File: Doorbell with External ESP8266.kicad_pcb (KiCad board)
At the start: 4 copper layers, 76.2 x 50.8 mm, 29 parts, among them J101 Rectifier, J105 Transformer, J106 Button, J107 Chime, K102 Relay, Q102 Q_NMOS_GSD, U101 WeMos_D1_mini, U102 EL817, U104 XC6220B331MR-G

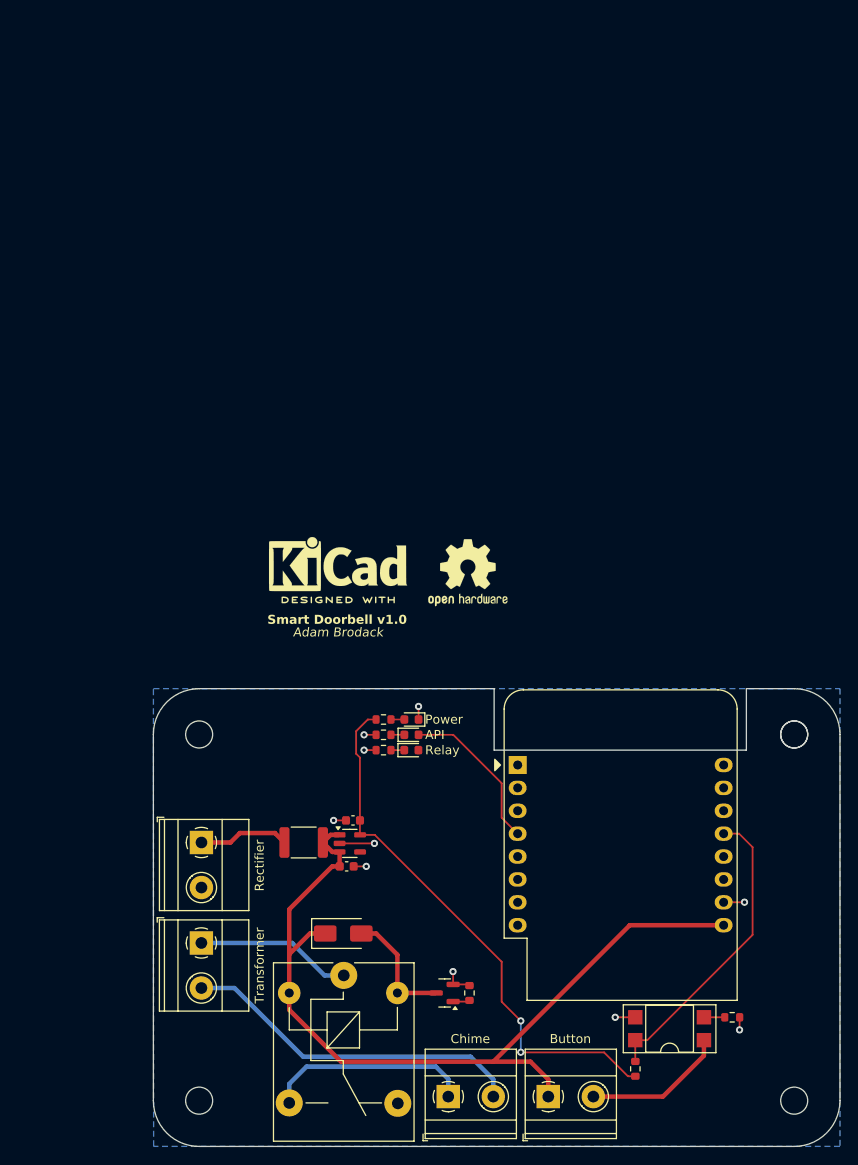
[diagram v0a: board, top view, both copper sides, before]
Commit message: Removed CHIME & improved wiring
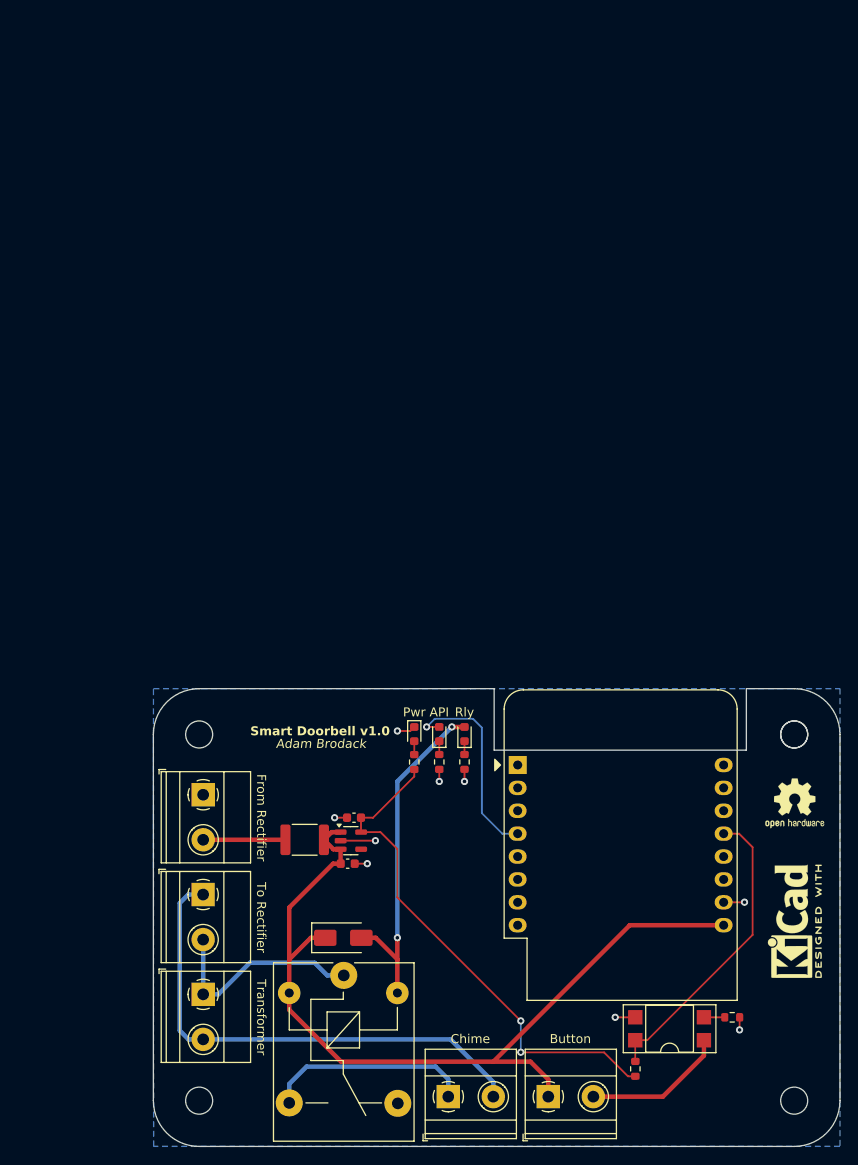
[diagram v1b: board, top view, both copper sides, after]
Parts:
- removed J106: Button, TerminalBlock_Phoenix:TerminalBlock_Phoenix_MKDS-1,5-2_1x02_P5.00mm_Horizontal
- removed J107: Chime, TerminalBlock_Phoenix:TerminalBlock_Phoenix_MKDS-1,5-2_1x02_P5.00mm_Horizontal
- removed Q102: Q_NMOS_GSD, Package_TO_SOT_SMD:SOT-23
- removed R107: 10K, Resistor_SMD:R_0603_1608Metric
- removed the REF** at (55.5, 80.4)
- removed the REF** at (69.9, 81.3)
- added J102: To Rectifier, TerminalBlock_Phoenix:TerminalBlock_Phoenix_MKDS-1,5-2_1x02_P5.00mm_Horizontal, F.Cu at (40.5, 117.1)
- added J103: From Rectifier, TerminalBlock_Phoenix:TerminalBlock_Phoenix_MKDS-1,5-2_1x02_P5.00mm_Horizontal, F.Cu at (40.5, 106.0)
- added J104: Button, TerminalBlock_Phoenix:TerminalBlock_Phoenix_MKDS-1,5-2_1x02_P5.00mm_Horizontal, F.Cu at (78.8, 139.5)
- added REF**: OSHW-Logo2_7.3x6mm_SilkScreen, Symbol:OSHW-Logo2_7.3x6mm_SilkScreen, F.Cu at (106.2, 107.0)
- added REF**: KiCad-Logo2_5mm_SilkScreen, Symbol:KiCad-Logo2_5mm_SilkScreen, F.Cu at (106.2, 120.0)
- J101: value Rectifier -> Transformer
- J105: value Transformer -> Chime
- moved J105 32.3 mm to (67.7, 139.5), turned to 0 degrees
- moved J101 16.9 mm to (40.5, 128.2)
- moved R103 9.08 mm to (69.5, 102.4), turned to 90 degrees
- moved R102 6.88 mm to (66.7, 102.4), turned to 90 degrees
- moved D106 6.16 mm to (69.5, 99.3), turned to 90 degrees
- moved R101 5.82 mm to (63.9, 102.4), turned to -90 degrees
- moved D105 3.09 mm to (66.7, 99.3), turned to 90 degrees
- moved D104 1.65 mm to (63.9, 99.3), turned to -90 degrees
- moved D101 0.47 mm to (56.0, 121.9)
- moved U104 0.32 mm to (56.9, 111.1)
- moved C105 0.32 mm to (56.5, 113.7)
- moved F101 0.32 mm to (51.8, 111.0)
- moved C106 0.32 mm to (57.2, 108.5)
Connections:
- F101 pad 1: Net-(J101-Pin_1) -> Net-(J103-Pin_2)
- J101 pad 1: Net-(J101-Pin_1) -> /AC_A
- J101 pad 2: GND -> /AC_B
- J105 pad 2: Net-(J105-Pin_2) -> /AC_B
- K102 pad 1: Net-(J105-Pin_1) -> /AC_A
- K102 pad 3: Net-(J107-Pin_1) -> Net-(J105-Pin_1)
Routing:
- net /AC_B: track 0.00 -> 55.9 mm
- net Net-(J105-Pin_2): track 38.5 -> 0.00 mm
- net /RELAY_LED: track 13.5 -> 38.4 mm, vias 0 -> 2
- net /AC_A: track 0.00 -> 23.7 mm
- net Net-(J107-Pin_1): track 23.1 -> 0.00 mm
- net Net-(J101-Pin_1): track 10.1 -> 0.00 mm
- net Net-(J103-Pin_2): track 0.00 -> 9.12 mm
- net Net-(J105-Pin_1): track 17.3 -> 23.1 mm
- net /HA_STATUS: track 17.8 -> 22.7 mm, vias 0 -> 1
- net +3V3: track 60.7 -> 57.0 mm
- net GND: track 20.0 -> 17.3 mm, vias 10 -> 9
- net /CHIME: track 1.86 -> 0.00 mm
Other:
- board text added: "From Rectifier"
- board text added: "Pwr"
- board text added: "Rly"
- board text added: "To Rectifier"
- board text removed: "Power"
- board text removed: "Rectifier"
- board text removed: "Relay"

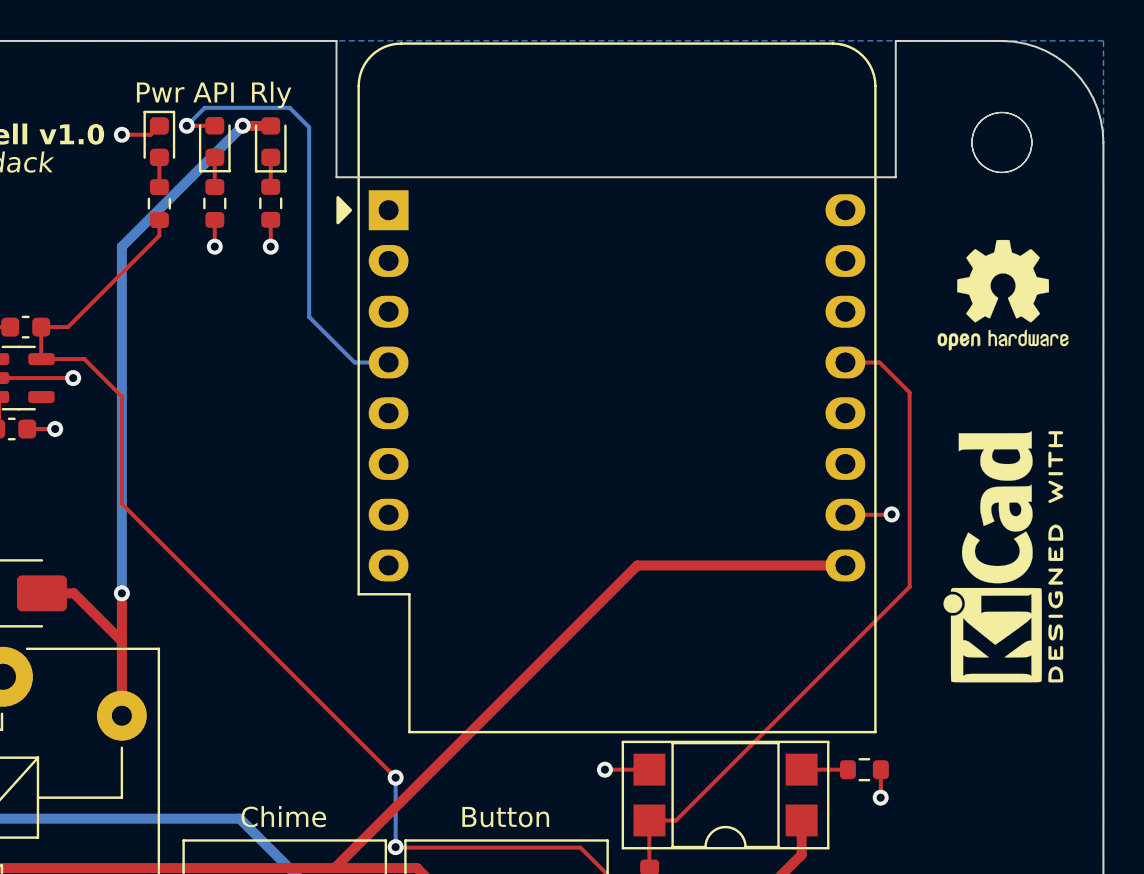
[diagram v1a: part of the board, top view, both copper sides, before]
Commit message: Added ability to control chime from ESP8266
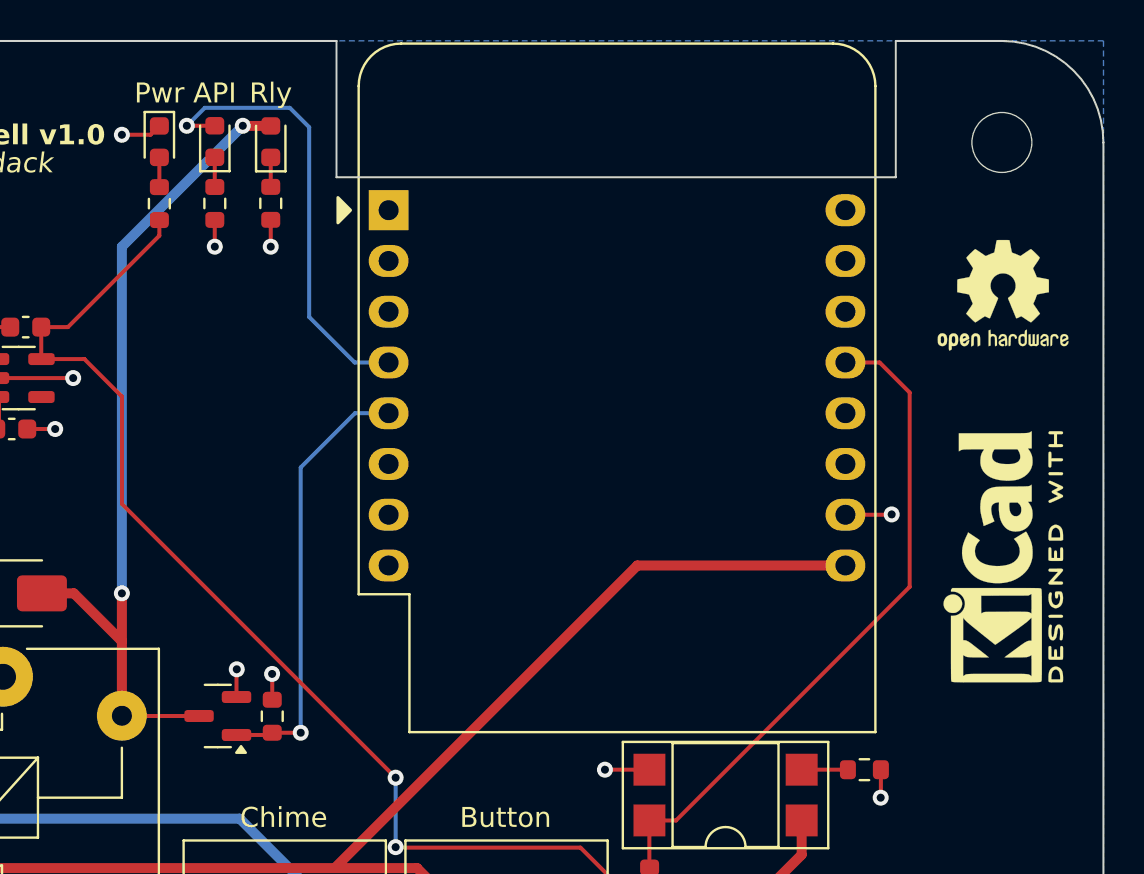
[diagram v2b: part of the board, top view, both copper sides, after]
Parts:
- removed ?: , 
- added Q101: Q_NMOS_GSD, Package_TO_SOT_SMD:SOT-23, F.Cu at (66.8, 128.0)
- added R104: 10K, Resistor_SMD:R_0603_1608Metric, F.Cu at (69.6, 128.0)
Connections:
- U101 pad 5: unconnected-(U101-MISO/D6-Pad5) -> /CHIME
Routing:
- net /CHIME: track 0.00 -> 22.1 mm, vias 0 -> 1
- net /RELAY_LED: track 38.4 -> 42.3 mm
- net GND: track 17.3 -> 20.0 mm, vias 9 -> 11

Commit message: Updated schematic & PCB
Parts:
- removed C105: 22uF, Capacitor_SMD:C_0603_1608Metric
- removed C106: 4.7uF, Capacitor_SMD:C_0603_1608Metric
- removed D106: Yellow, LED_SMD:LED_0603_1608Metric
- removed K102: Relay, Relay_THT:Relay_SPDT_SANYOU_SRD_Series_Form_C
- removed R108: 10K, Resistor_SMD:R_0603_1608Metric
- removed U104: XC6220B331MR-G, Package_TO_SOT_SMD:SOT-23-5
- added C101: 22uF, Capacitor_SMD:C_0603_1608Metric, F.Cu at (41.1, 38.9)
- added C102: 4.7uF, Capacitor_SMD:C_0603_1608Metric, F.Cu at (41.9, 33.9)
- added D102: Green, LED_SMD:LED_0805_2012Metric, F.Cu at (46.8, 27.2)
- added D103: Yellow, LED_SMD:LED_0805_2012Metric, F.Cu at (46.8, 25.1)
- added K101: Relay, Relay_THT:Relay_SPDT_SANYOU_SRD_Series_Form_C, F.Cu at (44.0, 50.2)
- added R105: 10K, Resistor_SMD:R_0603_1608Metric, F.Cu at (50.6, 43.3)
- added R107: 10K, Resistor_SMD:R_0603_1608Metric, F.Cu at (72.6, 45.6)
- added U103: EL817, Package_DIP:DIP-4_W7.62mm_SMDSocket_SmallPads, F.Cu at (69.6, 49.3)
- D101: value D_Small -> Red; footprint Diode_SMD:D_SMA -> LED_SMD:LED_0805_2012Metric
- D104: value Red -> White; footprint LED_SMD:LED_0603_1608Metric -> LED_SMD:LED_0805_2012Metric
- D105: value Green -> D_Small; footprint LED_SMD:LED_0603_1608Metric -> Diode_SMD:D_SMA
- J102: value To Rectifier -> From Rectifier
- J103: value From Rectifier -> To Rectifier
- J104: value Button -> Chime
- J105: value Chime -> Button
- R104: value 10K -> 1K
- U102: value EL817 -> XC6220B331MR-G; footprint Package_DIP:DIP-4_W7.62mm_SMDSocket_SmallPads -> Package_TO_SOT_SMD:SOT-23-5
- moved REF** 118.7 mm to (35.2, 24.9), turned to 0 degrees
- moved U102 108.2 mm to (41.5, 36.4), turned to 0 degrees
- moved R104 102.1 mm to (43.5, 29.3), turned to 180 degrees
- moved D101 99.3 mm to (46.8, 23.0), turned to 180 degrees
- moved J101 98.0 mm to (25.7, 31.3)
- moved R106 84.3 mm to (66.6, 53.0), turned to 180 degrees
- moved Q101 83.8 mm to (50.5, 45.8)
- moved R101 82.0 mm to (43.5, 23.0), turned to 180 degrees
- moved R103 81.5 mm to (43.5, 25.1), turned to 180 degrees
- moved R102 78.7 mm to (43.5, 27.2), turned to 0 degrees
- moved J104 78.5 mm to (56.2, 64.3)
- moved H104 77.9 mm to (85.0, 65.0)
- moved H102 77.2 mm to (85.0, 25.0)
- moved U101 77.1 mm to (55.6, 28.2)
- moved H103 76.4 mm to (25.0, 65.0)
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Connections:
- D101 pad 1: VCC -> GND
- D101 pad 2: /RELAY_LED -> Net-(D101-A)
- D104 pad 1: GND -> /RELAY_LED
- D105 pad 1: Net-(D105-K) -> VCC
- D105 pad 2: /HA_STATUS -> /RELAY_LED
- F101 pad 1: Net-(J103-Pin_2) -> Net-(J102-Pin_2)
- J102 pad 1: /AC_B -> GND
- J102 pad 2: /AC_A -> Net-(J102-Pin_2)
- J103 pad 1: GND -> /AC_A
- J103 pad 2: Net-(J103-Pin_2) -> /AC_B
- J104 pad 1: VCC -> Net-(J104-Pin_1)
- J104 pad 2: Net-(J104-Pin_2) -> /AC_B
- J105 pad 2: /AC_B -> GND
- Q101 pad 1: /CHIME -> GND
- Q101 pad 2: GND -> /CHIME
- R101 pad 1: Net-(D104-A) -> Net-(D101-A)
- R102 pad 2: Net-(D105-K) -> Net-(D102-K)
- R103 pad 1: GND -> Net-(D103-A)
- R103 pad 2: Net-(D106-K) -> +3V3
- R104 pad 1: /CHIME -> Net-(D104-A)
- R104 pad 2: GND -> +3V3
- R106 pad 1: Net-(R106-Pad1) -> Net-(J105-Pin_1)
- R106 pad 2: GND -> Net-(R106-Pad2)
- U101 pad 16: unconnected-(U101-TX-Pad16) -> /ESP_TX
- U102 pad 1: Net-(J104-Pin_2) -> VCC
- U102 pad 2: Net-(R106-Pad1) -> GND
- U102 pad 3: GND -> VCC
- U102 pad 4: /DB_BUTTON -> unconnected-(U102-NC-Pad4)
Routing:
- net /ESP_TX: track 0.00 -> 33.8 mm
- net VCC: track 95.9 -> 69.8 mm, vias 0 -> 2
- net /AC_A: track 23.7 -> 44.2 mm
- net Net-(J104-Pin_1): track 0.00 -> 20.2 mm
- net Net-(J102-Pin_2): track 0.00 -> 19.8 mm
- net /DB_BUTTON: track 33.8 -> 15.1 mm
- net Net-(J104-Pin_2): track 15.9 -> 0.00 mm
- net /CHIME: track 22.1 -> 9.24 mm, vias 1 -> 0
- net Net-(J105-Pin_1): track 23.1 -> 11.3 mm
- net /RELAY_LED: track 42.3 -> 32.6 mm, vias 2 -> 0
- net Net-(J103-Pin_2): track 9.12 -> 0.00 mm
- net /HA_STATUS: track 22.7 -> 14.1 mm, vias 1 -> 0
- net +3V3: track 57.0 -> 51.3 mm
- net /AC_B: track 55.9 -> 59.4 mm
- net GND: track 20.0 -> 17.4 mm, vias 11 -> 9
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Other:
- board size 76.2 x 50.8 mm -> 70 x 50 mm
- board text added: "Act"

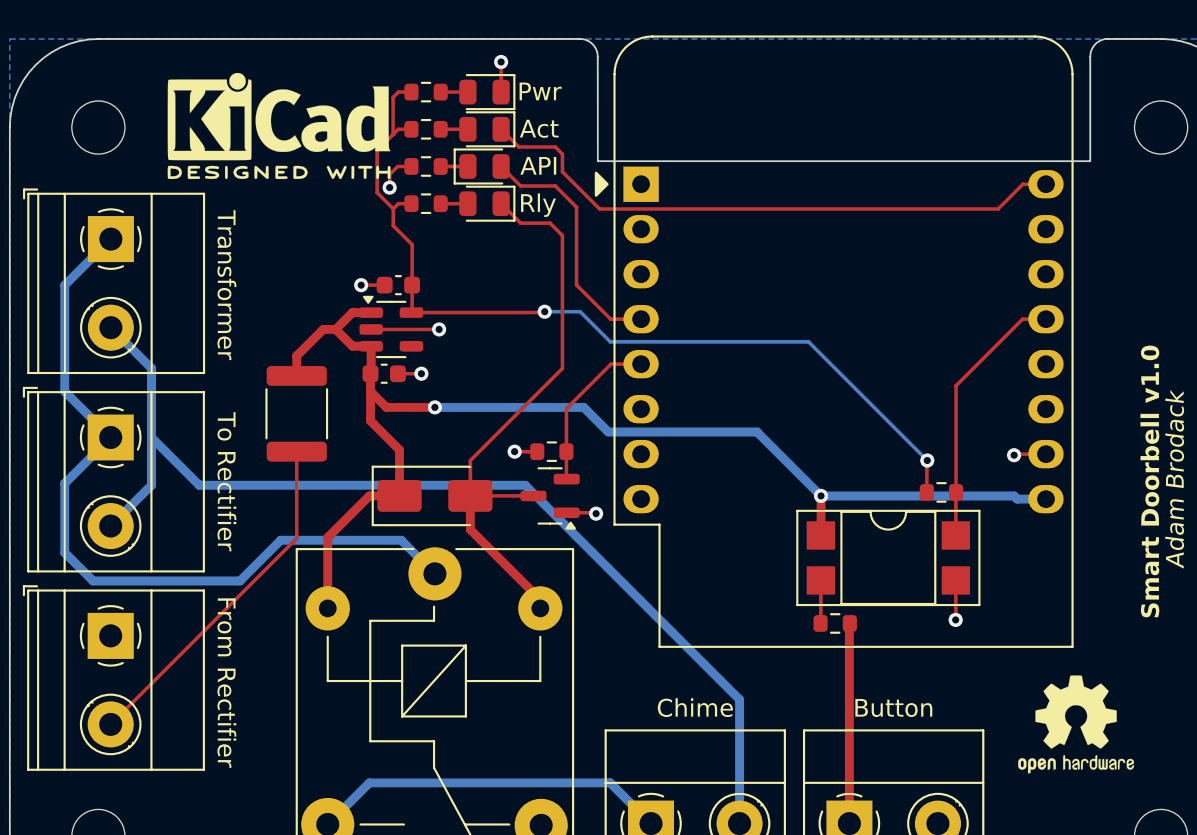
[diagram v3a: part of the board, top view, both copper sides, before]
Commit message: Improved the location for the LEDs & increased trace size for power from rectifier
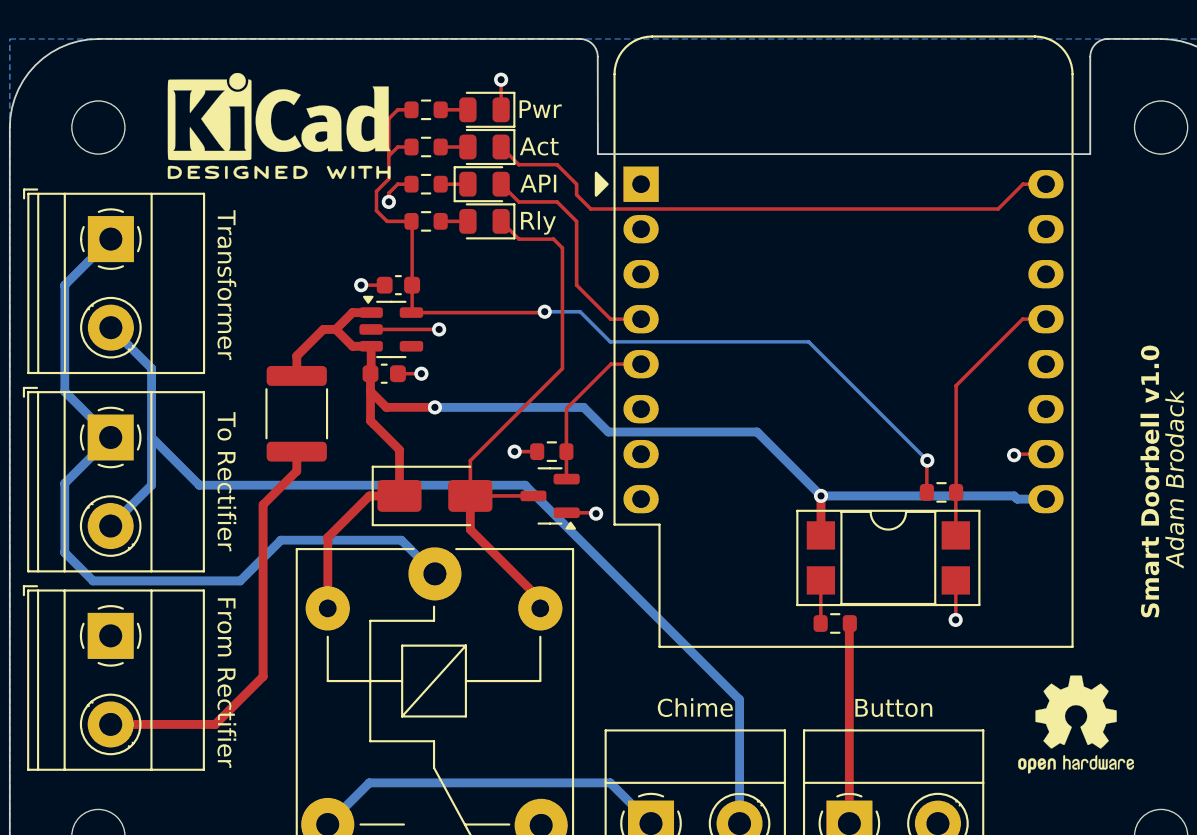
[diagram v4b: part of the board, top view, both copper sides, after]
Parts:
- moved D101 1.00 mm to (46.8, 24.0)
- moved D102 1.00 mm to (46.8, 28.2)
- moved D103 1.00 mm to (46.8, 26.1)
- moved D104 1.00 mm to (46.8, 30.3)
- moved R101 1.00 mm to (43.5, 24.0)
- moved R102 1.00 mm to (43.5, 28.2)
- moved R103 1.00 mm to (43.5, 26.1)
- moved R104 1.00 mm to (43.5, 30.3)
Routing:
- net Net-(J102-Pin_2): track 19.8 -> 23.2 mm
- net +3V3: track 51.3 -> 50.3 mm
- net /HA_STATUS: track 14.1 -> 13.2 mm
- net /RELAY_LED: track 32.6 -> 31.8 mm
- net /ESP_TX: track 33.8 -> 33.1 mm
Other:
- outline, holes or cut-outs redrawn
